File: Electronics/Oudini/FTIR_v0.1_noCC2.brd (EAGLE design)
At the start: 80.2 x 84.6 mm, 96 parts, among them CON1 SPI, Q1 IRF3704S, Q3 IRF3704S, Q4 BSP75, Q7 IRF3704S, Q8 BSP75, X3 16MHz, X4 MINI-USB

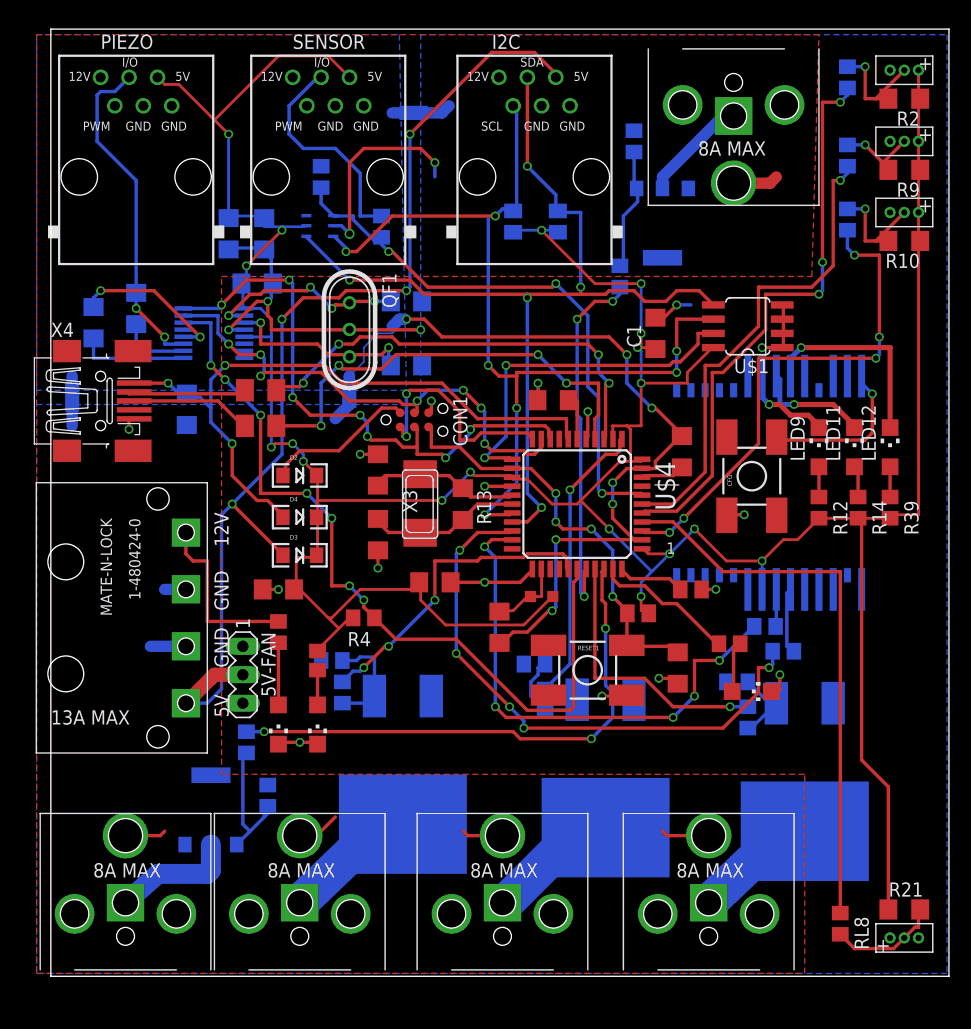
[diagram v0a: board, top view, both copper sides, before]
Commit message: finalisation of main FTIR board (Oudini)
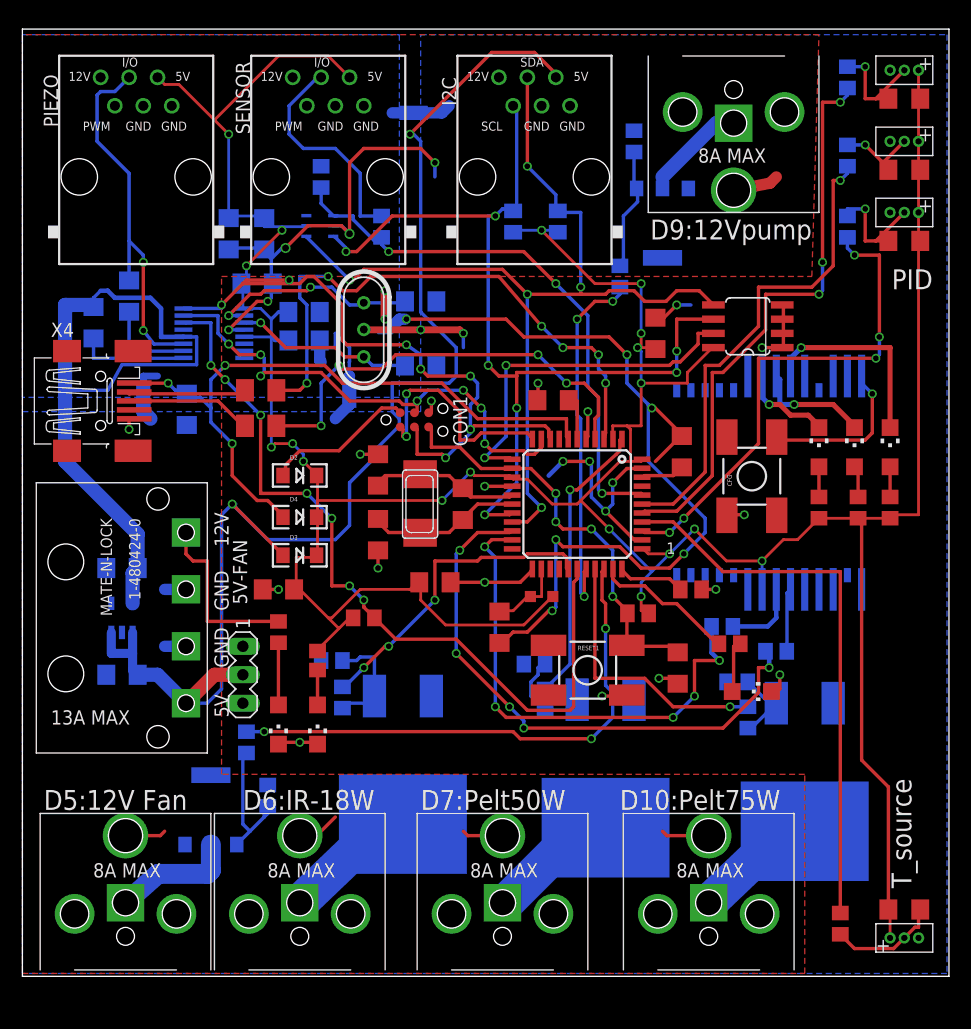
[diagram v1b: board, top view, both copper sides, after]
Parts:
- added C19: 100nF, rcl:C1206
- added C4, C5: 1uF, rcl:C1206
- added C6: 10uF, rcl:C1206
- added IC1: LP5907, v-reg:SOT25
- moved U$20 6.35 mm to (8.89, 48.9)
- moved R11 3.81 mm to (61.2, 28.4)
- moved C15 1.27 mm to (8.26, 57.9)
- moved QF1 1.27 mm to (29.2, 54.9)
- moved C20 1.27 mm to (34.3, 57.5)
- moved C21 1.27 mm to (34.3, 51.8)
- moved R8 0.64 mm to (66.0, 26.2)
- moved U$19 0.64 mm to (62.2, 79.4)
- moved RL6 0.63 mm to (72.4, 64.1)
- moved RL10 0.44 mm to (27.3, 22.1)
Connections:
- net +5V: now also C4.2, IC1.1, IC1.3
- net +5V/1: now also C19.2, C6.2
- net 2.5V: now also C5.1, IC1.5
- net AGND: now also C19.1, C6.1
- net GND: now also C4.1, C5.2, IC1.2, IC1.4
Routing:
- net 2.5V: track 13.8 -> 61.2 mm, vias 2 -> 0
- net +5V: track 95.4 -> 120.8 mm, vias 4 -> 2
- net GND: track 106.5 -> 127.3 mm, vias 22 -> 28
- net AGND: track 77.2 -> 96.2 mm, vias 7 -> 8
- net USB_N: track 39.9 -> 51.4 mm, vias 4 -> 6
- net SCK: track 51.8 -> 60.0 mm
- net +5V/1: track 318.8 -> 325.0 mm
- net PIEZO: track 29.9 -> 33.9 mm
- net N$11: track 3.32 -> 6.73 mm
- net N$15: track 6.63 -> 8.37 mm
- net N$19: track 17.4 -> 15.9 mm, vias 2 -> 1
- net TX: track 46.1 -> 45.1 mm
- net D6*: track 28.0 -> 28.9 mm
- net N$31: track 18.2 -> 19.0 mm, vias 4 -> 2
- net SDA: track 85.7 -> 86.5 mm
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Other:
- board size 80.2 x 84.6 mm -> 82.7 x 84.6 mm
- board text added: "D10:Pelt75W"
- board text added: "D5:12V Fan"
- board text added: "D6:IR-18W"
- board text added: "D7:Pelt50W"
- board text added: "D9:12Vpump"
- board text added: "PID"
- board text added: "T_source"

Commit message: finished sensor board for D205B, finished main board Oudini v1.0, Generated Gerbers, modified CAD for PCB support
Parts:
- removed U$2, U$20: STARGND, lpatiny:STAR
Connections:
- net AGND: now also PIEZO.PWM, SENSOR.PWM; no longer U$2.AGND, U$20.AGND
- net GND: now also U$15.VIN-; no longer U$2.DGND, U$2.GND, U$20.DGND, U$20.GND
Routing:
- net N$30: track 11.7 -> 16.5 mm
- net GND: track 127.3 -> 122.7 mm
- net +5V: track 120.8 -> 119.3 mm, vias 2 -> 1
- net AGND: track 96.2 -> 96.6 mm, vias 8 -> 6
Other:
- board size 82.7 x 84.6 mm -> 82 x 87.6 mm
- board text added: "Oudini v1.0 06.08.2015"
